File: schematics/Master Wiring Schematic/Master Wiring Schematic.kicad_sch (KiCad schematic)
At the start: 11 parts, among them J1 M5_Ring_Terminals, J2 Raspberry_Pi_4, J3 USB_A, J4 USB_B

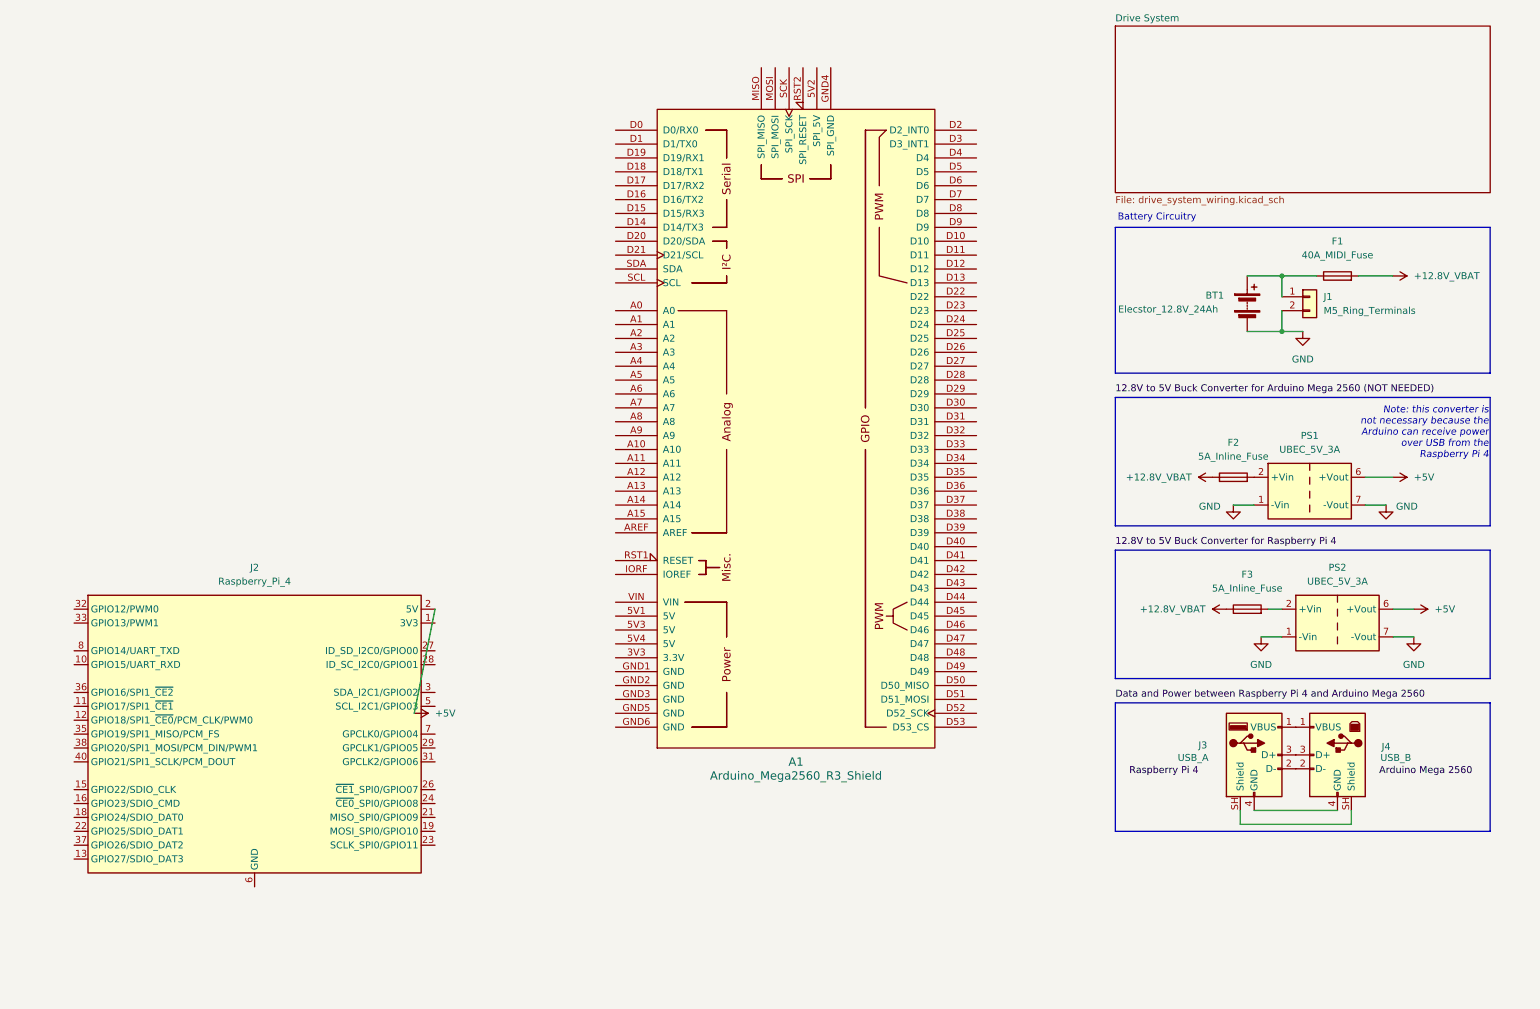
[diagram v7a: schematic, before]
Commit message: Drive system components are being laid out on a subsheet
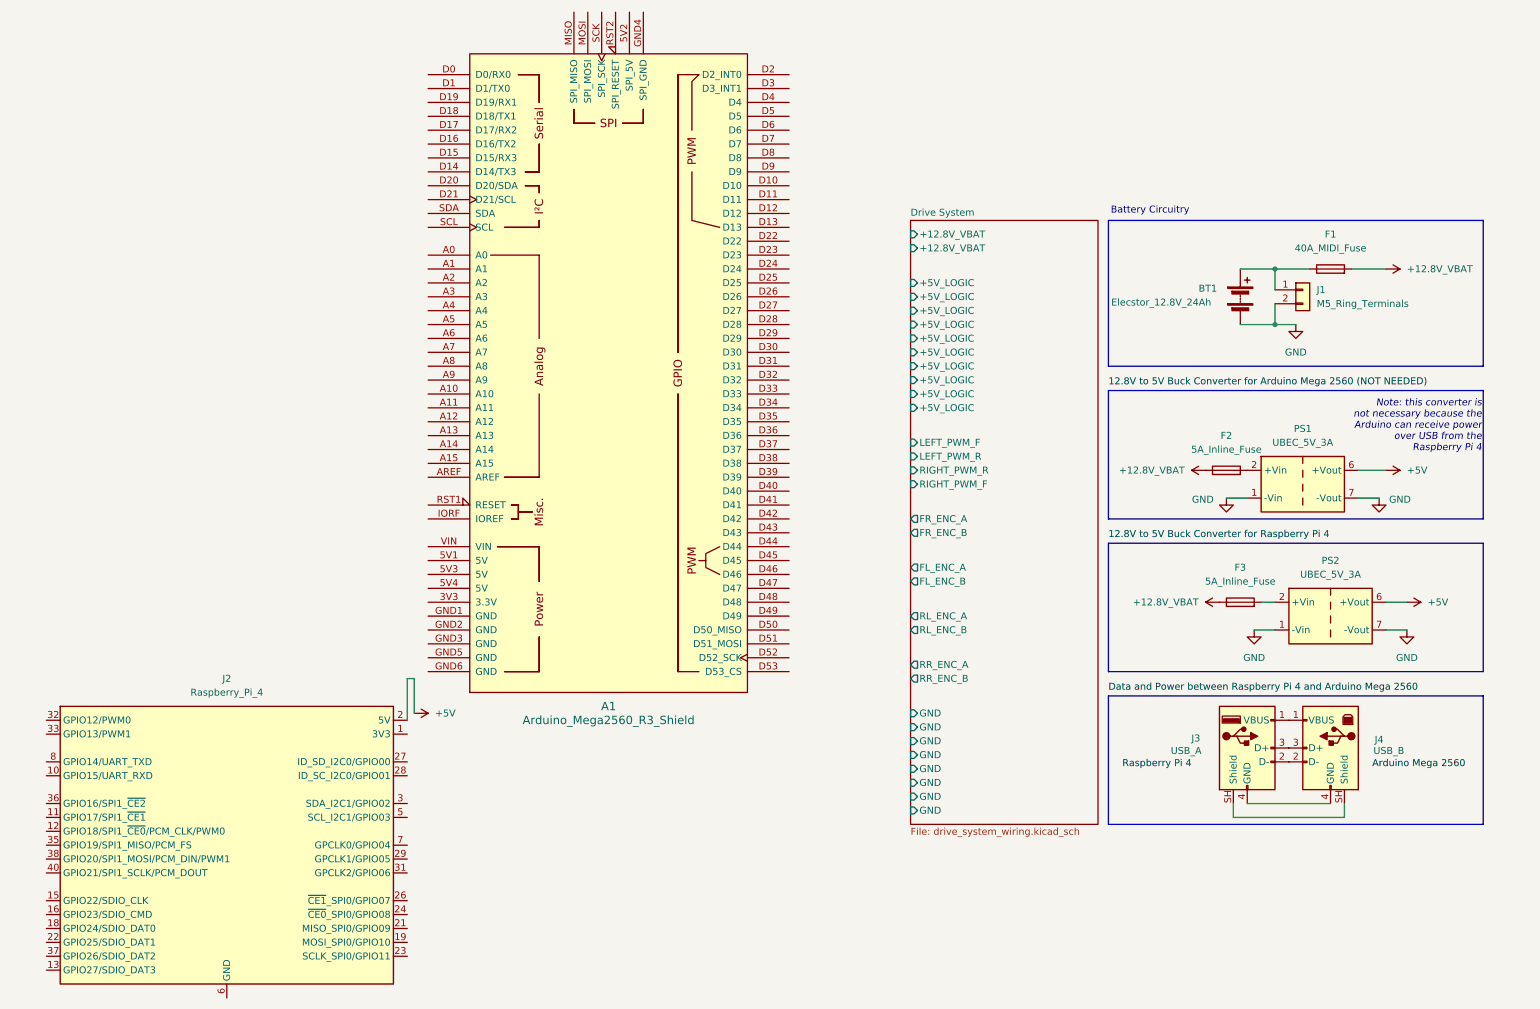
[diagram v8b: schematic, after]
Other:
- sheet Drive System ports: added +12.8V_VBAT, +5V_LOGIC, FL_ENC_A, FL_ENC_B, FR_ENC_A, FR_ENC_B, GND, LEFT_PWM_F, LEFT_PWM_R, RIGHT_PWM_F, RIGHT_PWM_R, RL_ENC_A, RL_ENC_B, RR_ENC_A, RR_ENC_B; removed none
- moved on the sheet: A1, BT1, F1, F2, F3, J1, J2, J3, J4, PS1, PS2
